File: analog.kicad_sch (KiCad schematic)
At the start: 37 parts

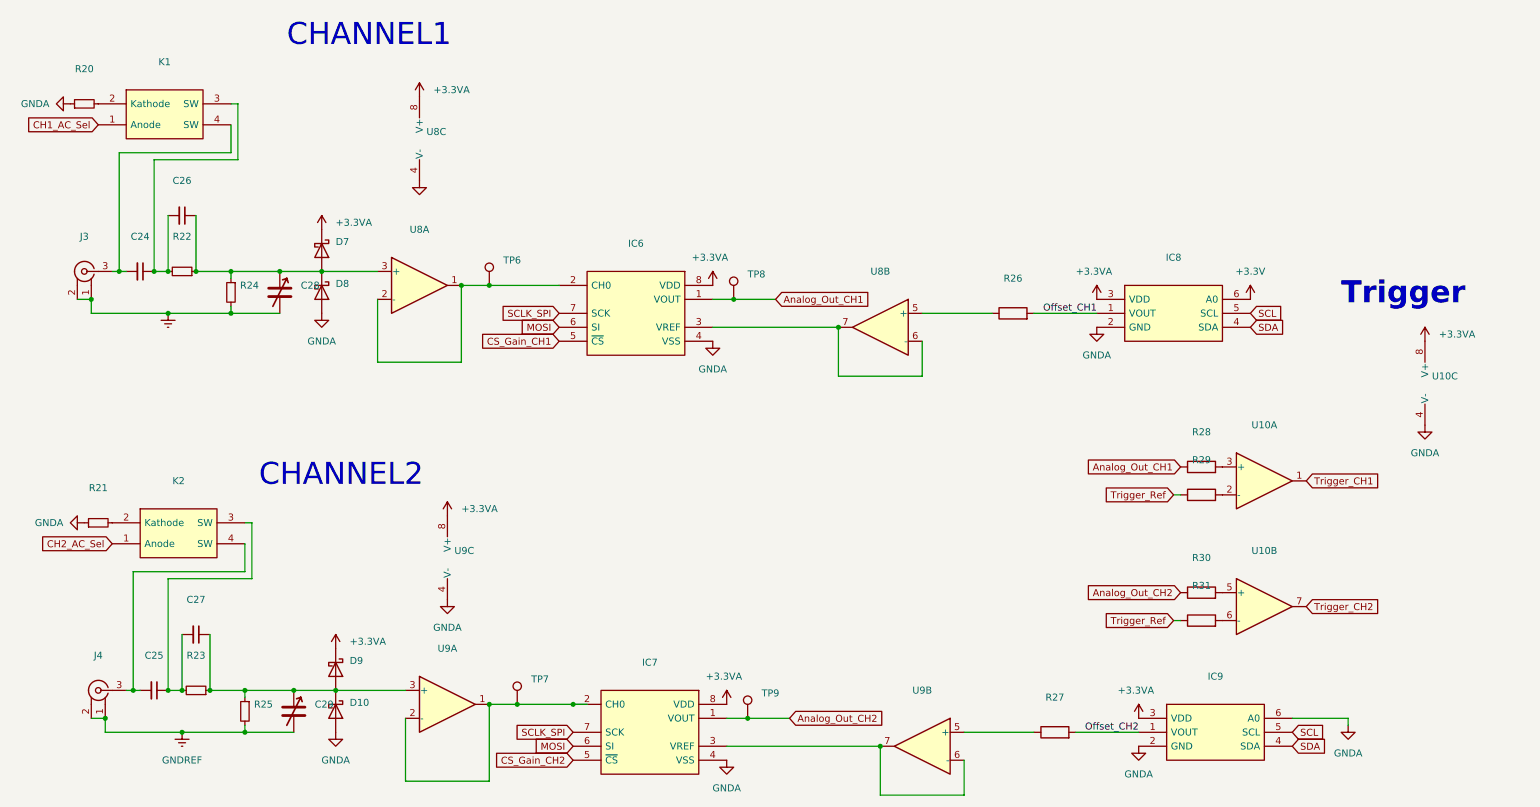
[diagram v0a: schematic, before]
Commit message: small fix for jlcpcb parts detection
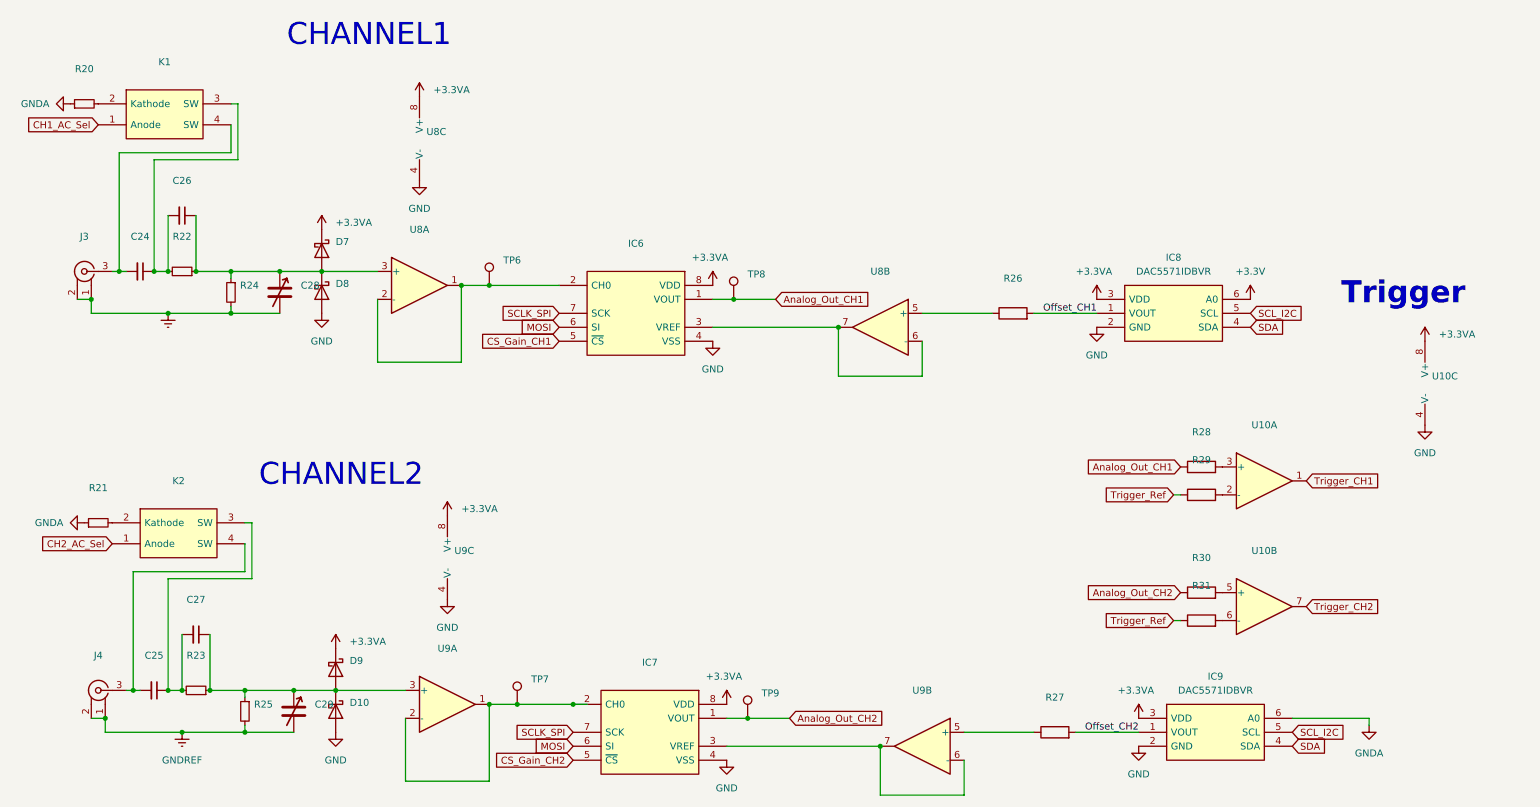
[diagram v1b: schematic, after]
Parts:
- C24, C25, C26, C27: value (none) -> ~; footprint (none) -> Capacitor_SMD:C_0805_2012Metric_Pad1.18x1.45mm_HandSolder
- C28, C29: value (none) -> ~; footprint (none) -> project_library:JZ300
- D10, D7, D8, D9: value (none) -> ~; footprint (none) -> Diode_SMD:D_0805_2012Metric_Pad1.15x1.40mm_HandSolder
- IC6, IC7, J3, J4, K1, K2: value (none) -> ~
- IC8, IC9: value (none) -> DAC5571IDBVR
- R20, R21, R22, R23, R24, R25, R26, R27, R28, R29, R30, R31: value (none) -> ~; footprint (none) -> Resistor_SMD:R_0805_2012Metric_Pad1.20x1.40mm_HandSolder
- TP6, TP7, TP8, TP9: value (none) -> ~; footprint (none) -> TestPoint:TestPoint_Keystone_5000-5004_Miniature
- U10, U8, U9: value (none) -> ~; footprint (none) -> project_library:MCP6022T-I_SN
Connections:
- net GNDA: no longer D10.2 (A), D8.2 (A), IC6.4 (VSS), IC7.4 (VSS), IC8.2 (GND), IC9.2 (GND), U10.4 (V-), U8.4 (V-), U9.4 (V-)
- net SCL renamed SCL_I2C
- new net GND: D10.2 (A), D8.2 (A), IC6.4 (VSS), IC7.4 (VSS), IC8.2 (GND), IC9.2 (GND), U10.4 (V-), U8.4 (V-), U9.4 (V-)

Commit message: Added ADC vor Trigger and changed Layout
Some Traces cant be good routed
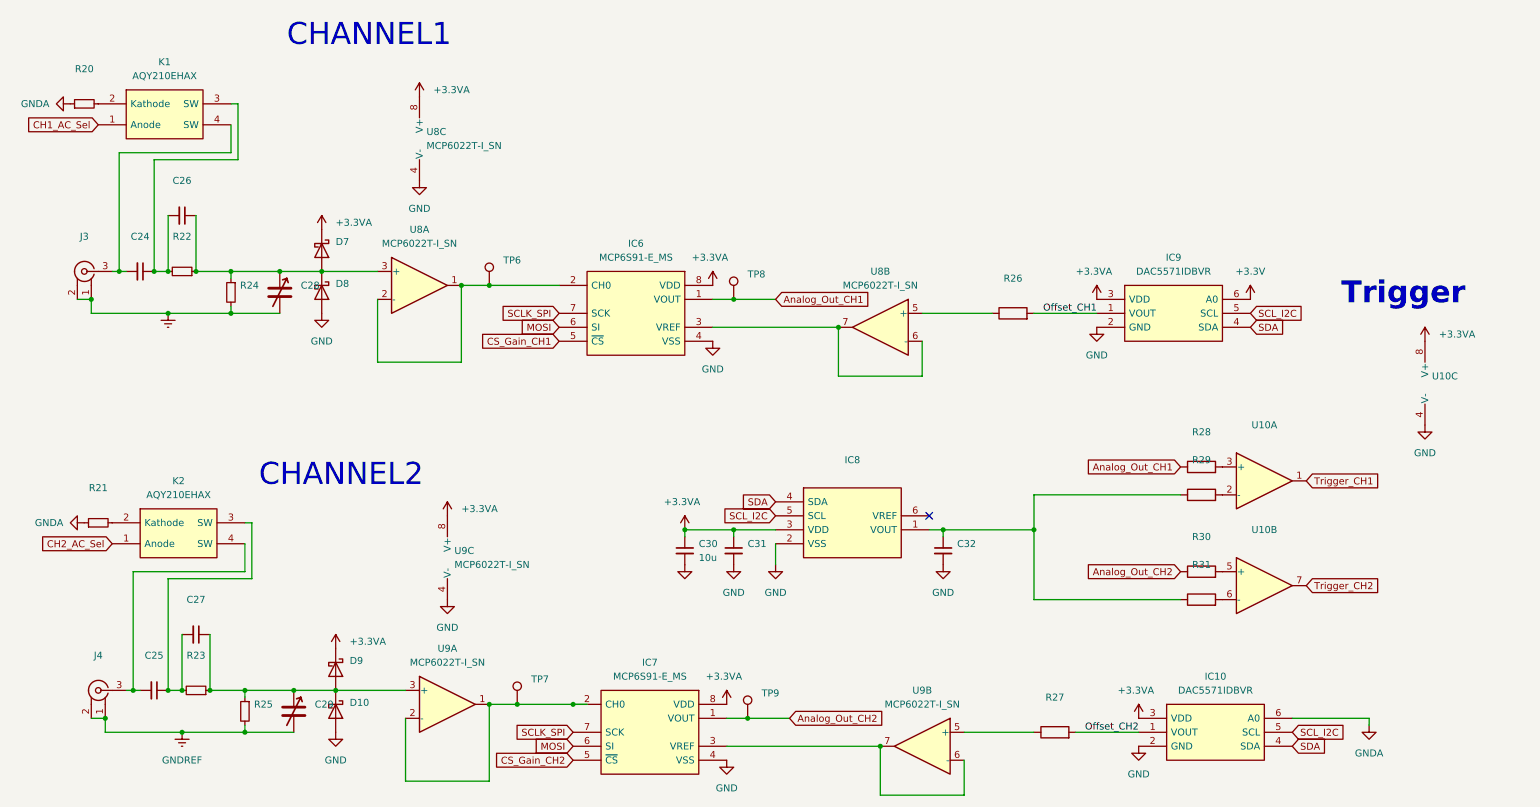
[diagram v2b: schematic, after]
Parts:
- added C30: 10u, Capacitor_SMD:C_0805_2012Metric_Pad1.18x1.45mm_HandSolder, symbol Device:C_Small
- added C31, C32: (no value), Capacitor_SMD:C_0805_2012Metric_Pad1.18x1.45mm_HandSolder, symbol Device:C_Small
- added IC8: (no value), symbol project_library:MCP4726A1T-E_CH
- IC6, IC7: value ~ -> MCP6S91-E_MS
- K1, K2: value ~ -> AQY210EHAX
- U10: value ~ -> (none); footprint project_library:MCP6022T-I_SN -> (none)
- U8, U9: value ~ -> MCP6022T-I_SN
- renumbered IC9 to IC10, IC8 to IC9
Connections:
- net +3.3VA: now also C30.1, C31.1, IC8.3 (VDD)
- net GND: now also C30.2, C31.2, C32.2, IC8.2 (VSS)
- net SCL_I2C: now also IC8.5 (SCL)
- net SDA: now also IC8.4 (SDA)
- net Trigger_Ref: no longer names the net of R29.1, R31.1
- net Trigger_Ref: now also C32.1, IC8.1 (VOUT)
- no-connect marks 0 -> 1
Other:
- moved on the sheet: R30, R31, U10B

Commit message: added values for analog front end
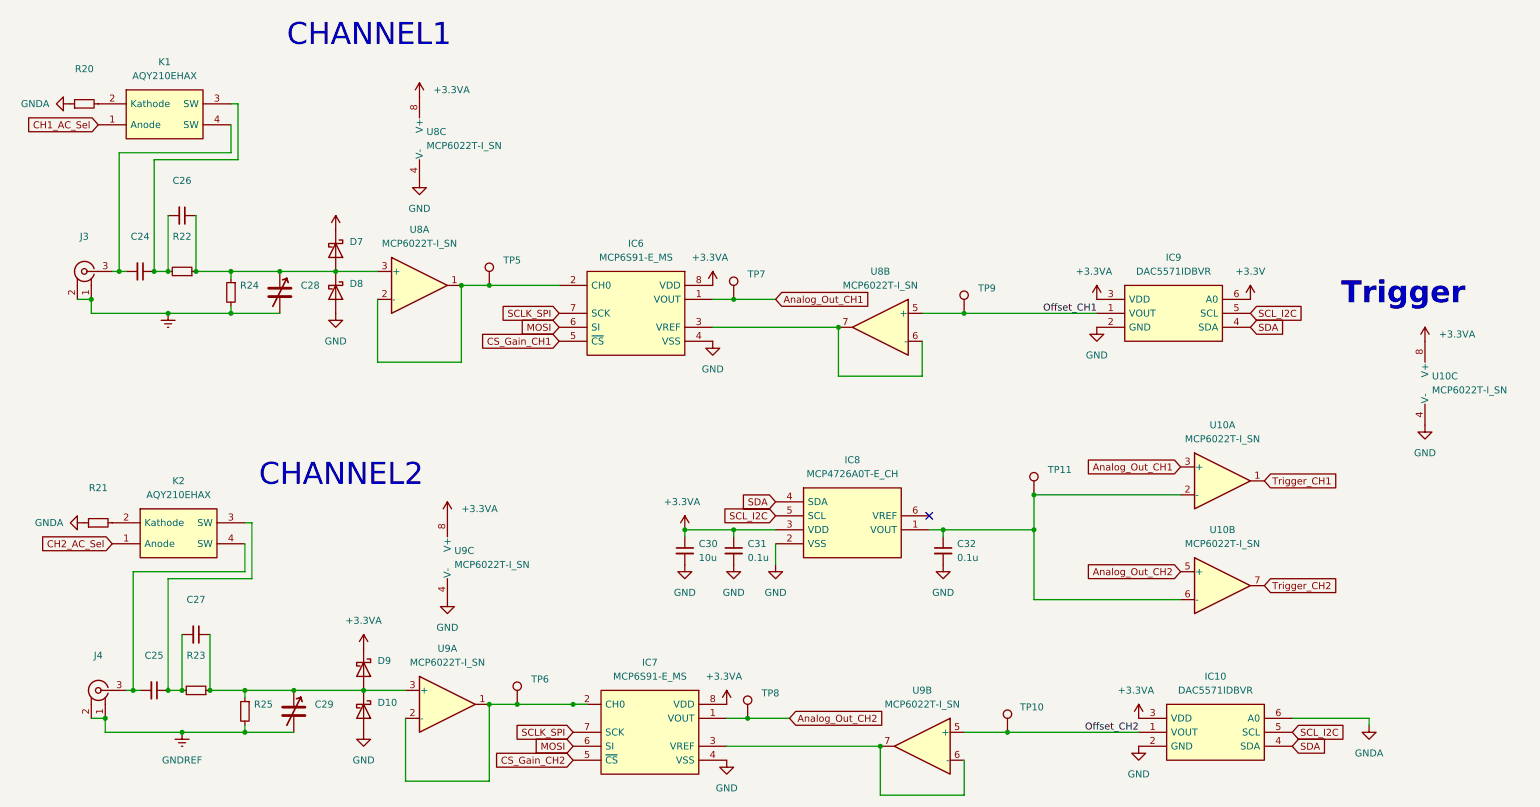
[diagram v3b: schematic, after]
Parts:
- removed R26, R27, R28, R29, R30, R31: ~, Resistor_SMD:R_0805_2012Metric_Pad1.20x1.40mm_HandSolder, symbol Device:R
- added TP10, TP11, TP9: (no value), TestPoint:TestPoint_Keystone_5000-5004_Miniature, symbol Connector:TestPoint
- C24, C25, C26, C27: value ~ -> (none); footprint Capacitor_SMD:C_0805_2012Metric_Pad1.18x1.45mm_HandSolder -> (none)
- C28, C29: value ~ -> (none); footprint project_library:JZ300 -> (none)
- C31, C32: value (none) -> 0.1u
- D10, D7, D8, D9: value ~ -> (none); footprint Diode_SMD:D_0805_2012Metric_Pad1.15x1.40mm_HandSolder -> (none)
- IC8: value (none) -> MCP4726A0T-E_CH; footprint (none) -> project_library:MCP4726A1T-E_CH
- R20, R21, R22, R23, R24, R25: value ~ -> (none); footprint Resistor_SMD:R_0805_2012Metric_Pad1.20x1.40mm_HandSolder -> (none)
- U10: value (none) -> MCP6022T-I_SN; footprint (none) -> project_library:MCP6022T-I_SN
- renumbered TP6 to TP5, TP7 to TP6, TP8 to TP7, TP9 to TP8
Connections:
- net Analog_Out_CH1: now also U10.3 (+)
- net Analog_Out_CH2: now also U10.5 (+)
- net Offset_CH1: now also U8.5 (+), TP9.1
- net Offset_CH2: now also U9.5 (+), TP10.1
- net at C32.1, IC8.1 (VOUT): now also U10.2 (-), U10.6 (-), TP11.1
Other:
- moved on the sheet: D10, D7, D8, D9, U10A, U10B

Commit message: new adc
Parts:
- C24, C25: value (none) -> 100n; footprint (none) -> Capacitor_SMD:C_0805_2012Metric_Pad1.18x1.45mm_HandSolder
- C26, C27: value (none) -> 5p; footprint (none) -> Capacitor_SMD:C_0805_2012Metric_Pad1.18x1.45mm_HandSolder
- C28, C29: value (none) -> Var_25p; footprint (none) -> project_library:JZ300
- D10, D7, D8, D9: value (none) -> D_Schottky; footprint (none) -> Diode_SMD:D_0805_2012Metric_Pad1.15x1.40mm_HandSolder
- R20, R21: value (none) -> 1k; footprint (none) -> Resistor_SMD:R_0805_2012Metric_Pad1.20x1.40mm_HandSolder
- R22, R23: value (none) -> 835k; footprint (none) -> Resistor_SMD:R_0805_2012Metric_Pad1.20x1.40mm_HandSolder
- R24, R25: value (none) -> 165k; footprint (none) -> Resistor_SMD:R_0805_2012Metric_Pad1.20x1.40mm_HandSolder
- TP10, TP11, TP9: value (none) -> ?
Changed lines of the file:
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@@
       (effects (font (size 1.27 1.27)) (justify left))
     )
-    (property "Value" "" (id 1) (at 62.23 147.32 0)
-      (effects (font (size 1.27 1.27)) (justify left))
-    )
-    (property "Footprint" "" (id 2) (at 55.88 146.05 0)
+    (property "Value" "165k" (id 1) (at 62.23 147.32 0)
+      (effects (font (size 1.27 1.27)) (justify left))
+    )
+    (property "Footprint" "Resistor_SMD:R_0805_2012Metric_Pad1.20x1.40mm_HandSolder" (id 2) (at 55.88 146.05 0)
       (effects (font (size 1.27 1.27)) hide)
     )
@@
       (effects (font (size 1.27 1.27)) (justify left))
     )
-    (property "Value" "" (id 1) (at 66.04 71.12 0)
-      (effects (font (size 1.27 1.27)) (justify left))
-    )
-    (property "Footprint" "" (id 2) (at 62.23 69.85 0)
+    (property "Value" "Var_25p" (id 1) (at 66.04 71.12 0)
+      (effects (font (size 1.27 1.27)) (justify left))
+    )
+    (property "Footprint" "project_library:JZ300" (id 2) (at 62.23 69.85 0)
       (effects (font (size 1.27 1.27)) hide)
     )
@@
     (in_bom yes) (on_board yes) (fields_autoplaced)
     (property "Reference" "R23" (id 0) (at 46.99 135.89 90))
-    (property "Value" "" (id 1) (at 46.99 138.43 90))
-    (property "Footprint" "" (id 2) (at 46.99 142.24 0)
+    (property "Value" "835k" (id 1) (at 46.99 138.43 90))
+    (property "Footprint" "Resistor_SMD:R_0805_2012Metric_Pad1.20x1.40mm_HandSolder" (id 2) (at 46.99 142.24 0)
       (effects (font (size 1.27 1.27)) hide)
     )
@@
       (effects (font (size 1.27 1.27)) (justify left))
     )
-    (property "Value" "" (id 1) (at 201.93 104.6479 0)
+    (property "Value" "?" (id 1) (at 201.93 104.6479 0)
       (effects (font (size 1.27 1.27)) (justify left))
     )
@@
       (effects (font (size 1.27 1.27)) (justify left))
     )
-    (property "Value" "" (id 1) (at 80.01 147.0024 90)
-      (effects (font (size 1.27 1.27)) (justify left))
-    )
-    (property "Footprint" "" (id 2) (at 77.47 146.05 0)
+    (property "Value" "D_Schottky" (id 1) (at 80.01 147.0024 90)
+      (effects (font (size 1.27 1.27)) (justify left))
+    )
+    (property "Footprint" "Diode_SMD:D_0805_2012Metric_Pad1.15x1.40mm_HandSolder" (id 2) (at 77.47 146.05 0)
       (effects (font (size 1.27 1.27)) hide)
     )
@@
       (effects (font (size 1.27 1.27)) (justify left))
     )
-    (property "Value" "" (id 1) (at 189.23 71.6279 0)
+    (property "Value" "?" (id 1) (at 189.23 71.6279 0)
       (effects (font (size 1.27 1.27)) (justify left))
     )
@@
       (effects (font (size 1.27 1.27)) (justify left))
     )
-    (property "Value" "" (id 1) (at 74.93 63.1824 90)
-      (effects (font (size 1.27 1.27)) (justify left))
-    )
-    (property "Footprint" "" (id 2) (at 72.39 62.23 0)
+    (property "Value" "D_Schottky" (id 1) (at 74.93 63.1824 90)
+      (effects (font (size 1.27 1.27)) (justify left))
+    )
+    (property "Footprint" "Diode_SMD:D_0805_2012Metric_Pad1.15x1.40mm_HandSolder" (id 2) (at 72.39 62.23 0)
       (effects (font (size 1.27 1.27)) hide)
     )
@@
     (in_bom yes) (on_board yes) (fields_autoplaced)
     (property "Reference" "R22" (id 0) (at 44.45 59.69 90))
-    (property "Value" "" (id 1) (at 44.45 62.23 90))
-    (property "Footprint" "" (id 2) (at 44.45 66.04 0)
+    (property "Value" "835k" (id 1) (at 44.45 62.23 90))
+    (property "Footprint" "Resistor_SMD:R_0805_2012Metric_Pad1.20x1.40mm_HandSolder" (id 2) (at 44.45 66.04 0)
       (effects (font (size 1.27 1.27)) hide)
     )
@@
       (effects (font (size 1.27 1.27)) hide)
     )
-    (property "Value" "" (id 1) (at 72.39 53.34 0))
+    (property "Value" "+3.3VA" (id 1) (at 72.39 53.34 0))
     (property "Footprint" "" (id 2) (at 72.39 58.42 0)
       (effects (font (size 1.27 1.27)) hide)
@@
     (in_bom yes) (on_board yes) (fields_autoplaced)
     (property "Reference" "C27" (id 0) (at 46.9837 125.73 90))
-    (property "Value" "" (id 1) (at 46.9837 128.27 90))
-    (property "Footprint" "" (id 2) (at 46.99 132.08 0)
+    (property "Value" "5p" (id 1) (at 46.9837 128.27 90))
+    (property "Footprint" "Capacitor_SMD:C_0805_2012Metric_Pad1.18x1.45mm_HandSolder" (id 2) (at 46.99 132.08 0)
       (effects (font (size 1.27 1.27)) hide)
     )
@@
     (in_bom yes) (on_board yes)
     (property "Reference" "R20" (id 0) (at 26.67 29.21 90))
-    (property "Value" "" (id 1) (at 26.67 31.75 90))
-    (property "Footprint" "" (id 2) (at 26.67 35.56 0)
+    (property "Value" "1k" (id 1) (at 26.67 31.75 90))
+    (property "Footprint" "Resistor_SMD:R_0805_2012Metric_Pad1.20x1.40mm_HandSolder" (id 2) (at 26.67 35.56 0)
       (effects (font (size 1.27 1.27)) hide)
     )
@@
     (in_bom yes) (on_board yes) (fields_autoplaced)
     (property "Reference" "C25" (id 0) (at 39.3637 135.89 90))
-    (property "Value" "" (id 1) (at 39.3637 138.43 90))
-    (property "Footprint" "" (id 2) (at 39.37 142.24 0)
+    (property "Value" "100n" (id 1) (at 39.3637 138.43 90))
+    (property "Footprint" "Capacitor_SMD:C_0805_2012Metric_Pad1.18x1.45mm_HandSolder" (id 2) (at 39.37 142.24 0)
       (effects (font (size 1.27 1.27)) hide)
     )
@@
       (effects (font (size 1.27 1.27)) (justify left))
     )
-    (property "Value" "" (id 1) (at 74.93 70.8024 90)
-      (effects (font (size 1.27 1.27)) (justify left))
-    )
-    (property "Footprint" "" (id 2) (at 72.39 69.85 0)
+    (property "Value" "D_Schottky" (id 1) (at 74.93 70.8024 90)
+      (effects (font (size 1.27 1.27)) (justify left))
+    )
+    (property "Footprint" "Diode_SMD:D_0805_2012Metric_Pad1.15x1.40mm_HandSolder" (id 2) (at 72.39 69.85 0)
       (effects (font (size 1.27 1.27)) hide)
     )
@@
     (in_bom yes) (on_board yes) (fields_autoplaced)
     (property "Reference" "C26" (id 0) (at 44.4437 49.53 90))
-    (property "Value" "" (id 1) (at 44.4437 52.07 90))
-    (property "Footprint" "" (id 2) (at 44.45 55.88 0)
+    (property "Value" "5p" (id 1) (at 44.4437 52.07 90))
+    (property "Footprint" "Capacitor_SMD:C_0805_2012Metric_Pad1.18x1.45mm_HandSolder" (id 2) (at 44.45 55.88 0)
       (effects (font (size 1.27 1.27)) hide)
     )
@@
       (effects (font (size 1.27 1.27)) (justify left))
     )
-    (property "Value" "" (id 1) (at 59.69 71.12 0)
-      (effects (font (size 1.27 1.27)) (justify left))
-    )
-    (property "Footprint" "" (id 2) (at 53.34 69.85 0)
+    (property "Value" "165k" (id 1) (at 59.69 71.12 0)
+      (effects (font (size 1.27 1.27)) (justify left))
+    )
+    (property "Footprint" "Resistor_SMD:R_0805_2012Metric_Pad1.20x1.40mm_HandSolder" (id 2) (at 53.34 69.85 0)
       (effects (font (size 1.27 1.27)) hide)
     )
@@
       (effects (font (size 1.27 1.27)) (justify left))
     )
-    (property "Value" "" (id 1) (at 80.01 139.3824 90)
-      (effects (font (size 1.27 1.27)) (justify left))
-    )
-    (property "Footprint" "" (id 2) (at 77.47 138.43 0)
+    (property "Value" "D_Schottky" (id 1) (at 80.01 139.3824 90)
+      (effects (font (size 1.27 1.27)) (justify left))
+    )
+    (property "Footprint" "Diode_SMD:D_0805_2012Metric_Pad1.15x1.40mm_HandSolder" (id 2) (at 77.47 138.43 0)
       (effects (font (size 1.27 1.27)) hide)
     )
@@
     (in_bom yes) (on_board yes)
     (property "Reference" "R21" (id 0) (at 29.21 105.41 90))
-    (property "Value" "" (id 1) (at 29.21 107.95 90))
-    (property "Footprint" "" (id 2) (at 29.21 111.76 0)
+    (property "Value" "1k" (id 1) (at 29.21 107.95 90))
+    (property "Footprint" "Resistor_SMD:R_0805_2012Metric_Pad1.20x1.40mm_HandSolder" (id 2) (at 29.21 111.76 0)
       (effects (font (size 1.27 1.27)) hide)
     )
@@
       (effects (font (size 1.27 1.27)) (justify left))
     )
-    (property "Value" "" (id 1) (at 196.85 147.8279 0)
+    (property "Value" "?" (id 1) (at 196.85 147.8279 0)
       (effects (font (size 1.27 1.27)) (justify left))
     )
@@
       (effects (font (size 1.27 1.27)) (justify left))
     )
-    (property "Value" "" (id 1) (at 68.58 147.32 0)
-      (effects (font (size 1.27 1.27)) (justify left))
-    )
-    (property "Footprint" "" (id 2) (at 64.77 146.05 0)
+    (property "Value" "Var_25p" (id 1) (at 68.58 147.32 0)
+      (effects (font (size 1.27 1.27)) (justify left))
+    )
+    (property "Footprint" "project_library:JZ300" (id 2) (at 64.77 146.05 0)
       (effects (font (size 1.27 1.27)) hide)
     )
@@
     (in_bom yes) (on_board yes) (fields_autoplaced)
     (property "Reference" "C24" (id 0) (at 36.8237 59.69 90))
-    (property "Value" "" (id 1) (at 36.8237 62.23 90))
-    (property "Footprint" "" (id 2) (at 36.83 66.04 0)
-      (effects (font (size 1.27 1.27)) hide)
-    )
+    (property "Value" "100n" (id 1) (at 36.8237 62.23 90))
+    (property "Footprint" "Capacitor_SMD:C_0805_2012Metric_Pad1.18x1.45mm_HandSolder" (id 2) (at 36.83 66.04 0)
+      (effects (font (size 1.27 1.27)) hide)
+    )
